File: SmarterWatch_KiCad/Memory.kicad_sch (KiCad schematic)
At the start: 7 parts, among them U12 M24C64-WMN6TP

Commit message: Clean Up
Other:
- moved on the sheet: J4, J5, R16, R17, R18

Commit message: order
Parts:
- removed J4, J5, J6: ~, Connector_Wire:SolderWirePad_1x01_SMD_2x4mm, symbol SmarterWatch_symbols_j:Solder_pad
- added U24, U25, U26: ~, symbol Custom:OpenJumper
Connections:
- net +3.3V: now also U24.1, U25.1, U26.1
- net at R17.2, U12.2 (A1): now also U25.2
- net at R16.2, U12.1 (A0): now also U26.2
- net at R18.2, U12.3 (A2): now also U24.2

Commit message: Minor Changes
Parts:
- renumbered R16 to R18, R17 to R19, R18 to R20, U26 to U12, U25 to U13, U24 to U14, U12 to U15
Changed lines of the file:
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@@
 		(dnp no)
 		(fields_autoplaced yes)
-		(property "Reference" "U26"
+		(property "Reference" "U12"
 			(at 120.65 73.66 0)
 			(effects
@@
 			(project "Smarter Watch Stuff"
 				(path "/52181fb0-1be8-41da-83b2-7d5a62778ff4/d294410d-228e-40f6-af22-786adbb6924d"
-					(reference "U26")
+					(reference "U12")
 					(unit 1)
 				)
@@
 		(dnp no)
 		(fields_autoplaced yes)
-		(property "Reference" "#PWR0101"
+		(property "Reference" "#PWR065"
 			(at 123.19 66.04 0)
 			(effects
@@
 			(project ""
 				(path "/52181fb0-1be8-41da-83b2-7d5a62778ff4/d294410d-228e-40f6-af22-786adbb6924d"
-					(reference "#PWR0101")
+					(reference "#PWR065")
 					(unit 1)
 				)
@@
 		(dnp no)
 		(fields_autoplaced yes)
-		(property "Reference" "#PWR061"
+		(property "Reference" "#PWR067"
 			(at 138.43 105.41 0)
 			(effects
@@
 			(project ""
 				(path "/52181fb0-1be8-41da-83b2-7d5a62778ff4/d294410d-228e-40f6-af22-786adbb6924d"
-					(reference "#PWR061")
+					(reference "#PWR067")
 					(unit 1)
 				)
@@
 		(dnp no)
 		(fields_autoplaced yes)
-		(property "Reference" "R17"
+		(property "Reference" "R19"
 			(at 114.3 85.09 90)
 			(effects
@@
 			(project "Smarter Watch Stuff"
 				(path "/52181fb0-1be8-41da-83b2-7d5a62778ff4/d294410d-228e-40f6-af22-786adbb6924d"
-					(reference "R17")
+					(reference "R19")
 					(unit 1)
 				)
@@
 		(dnp no)
 		(fields_autoplaced yes)
-		(property "Reference" "R16"
+		(property "Reference" "R18"
 			(at 114.3 82.55 90)
 			(effects
@@
 			(project ""
 				(path "/52181fb0-1be8-41da-83b2-7d5a62778ff4/d294410d-228e-40f6-af22-786adbb6924d"
-					(reference "R16")
+					(reference "R18")
 					(unit 1)
 				)
@@
 		(dnp no)
 		(fields_autoplaced yes)
-		(property "Reference" "#PWR060"
+		(property "Reference" "#PWR066"
 			(at 138.43 85.09 0)
 			(effects
@@
 			(project ""
 				(path "/52181fb0-1be8-41da-83b2-7d5a62778ff4/d294410d-228e-40f6-af22-786adbb6924d"
-					(reference "#PWR060")
+					(reference "#PWR066")
 					(unit 1)
 				)
@@
 		(dnp no)
 		(fields_autoplaced yes)
-		(property "Reference" "#PWR062"
+		(property "Reference" "#PWR068"
 			(at 154.94 93.98 0)
 			(effects
@@
 			(project "Smarter Watch Stuff"
 				(path "/52181fb0-1be8-41da-83b2-7d5a62778ff4/d294410d-228e-40f6-af22-786adbb6924d"
-					(reference "#PWR062")
+					(reference "#PWR068")
 					(unit 1)
 				)
@@
 		(dnp no)
 		(fields_autoplaced yes)
-		(property "Reference" "#PWR059"
+		(property "Reference" "#PWR064"
 			(at 102.87 91.44 0)
 			(effects
@@
 			(project "Smarter Watch Stuff"
 				(path "/52181fb0-1be8-41da-83b2-7d5a62778ff4/d294410d-228e-40f6-af22-786adbb6924d"
-					(reference "#PWR059")
+					(reference "#PWR064")
 					(unit 1)
 				)
@@
 		(dnp no)
 		(fields_autoplaced yes)
-		(property "Reference" "U24"
+		(property "Reference" "U14"
 			(at 135.89 73.66 0)
 			(effects
@@
 			(project "Smarter Watch Stuff"
 				(path "/52181fb0-1be8-41da-83b2-7d5a62778ff4/d294410d-228e-40f6-af22-786adbb6924d"
-					(reference "U24")
+					(reference "U14")
 					(unit 1)
 				)
@@
 		(dnp no)
 		(fields_autoplaced yes)
-		(property "Reference" "U12"
+		(property "Reference" "U15"
 			(at 140.5733 81.28 0)
 			(effects
@@
 			(project ""
 				(path "/52181fb0-1be8-41da-83b2-7d5a62778ff4/d294410d-228e-40f6-af22-786adbb6924d"
-					(reference "U12")
+					(reference "U15")
 					(unit 1)
 				)
@@
 		(on_board yes)
 		(dnp no)
-		(property "Reference" "R18"
+		(property "Reference" "R20"
 			(at 114.3 87.63 90)
 			(effects
@@
 			(project "Smarter Watch Stuff"
 				(path "/52181fb0-1be8-41da-83b2-7d5a62778ff4/d294410d-228e-40f6-af22-786adbb6924d"
-					(reference "R18")
+					(reference "R20")
 					(unit 1)
 				)
@@
 		(dnp no)
 		(fields_autoplaced yes)
-		(property "Reference" "U25"
+		(property "Reference" "U13"
 			(at 128.27 73.66 0)
 			(effects
@@
 			(project "Smarter Watch Stuff"
 				(path "/52181fb0-1be8-41da-83b2-7d5a62778ff4/d294410d-228e-40f6-af22-786adbb6924d"
-					(reference "U25")
-					(unit 1)
-				)
+					(reference "U13")
+					(unit 1)
+				)

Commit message: Footprint Stuff
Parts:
- U15: footprint Package_SO:SOIC-8_3.9x4.9mm_P1.27mm -> (none)
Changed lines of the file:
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@@
 			)
 		)
-		(property "Footprint" "Package_SO:SOIC-8_3.9x4.9mm_P1.27mm"
+		(property "Footprint" ""
 			(at 138.43 80.01 0)
 			(effects

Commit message: Foot
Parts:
- U15: footprint (none) -> Custom_Foot:SOIC127P600X175-8N
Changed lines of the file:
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@@
 			)
 		)
-		(property "Footprint" ""
+		(property "Footprint" "Custom_Foot:SOIC127P600X175-8N"
 			(at 138.43 80.01 0)
 			(effects

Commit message: Jumpers
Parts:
- U12, U13, U14: footprint (none) -> Custom_Foot:Jumper_NO
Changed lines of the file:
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@@
 			)
 		)
-		(property "Footprint" ""
+		(property "Footprint" "Custom_Foot:Jumper_NO"
 			(at 118.11 73.66 0)
 			(effects
@@
 			)
 		)
-		(property "Footprint" ""
+		(property "Footprint" "Custom_Foot:Jumper_NO"
 			(at 133.35 73.66 0)
 			(effects
@@
 			)
 		)
-		(property "Footprint" ""
+		(property "Footprint" "Custom_Foot:Jumper_NO"
 			(at 125.73 73.66 0)
 			(effects

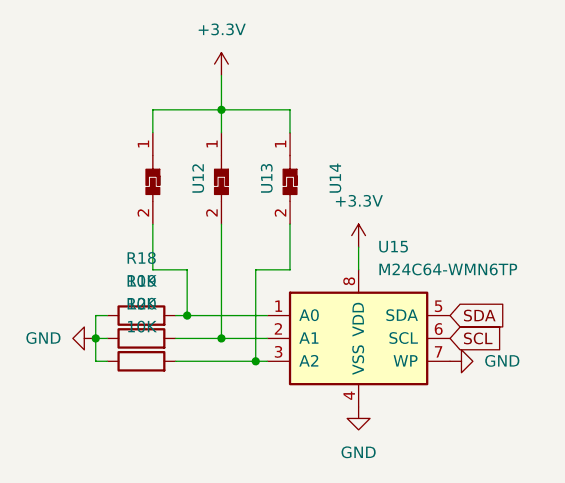
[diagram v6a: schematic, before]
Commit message: Label Jumpers
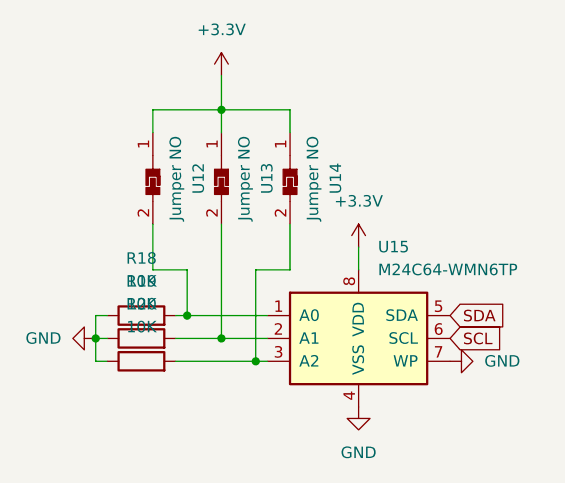
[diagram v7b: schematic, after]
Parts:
- U12, U13, U14: value ~ -> Jumper NO; footprint Custom_Foot:Jumper_NO -> (none)
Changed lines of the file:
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@@
 			)
 		)
-		(property "Value" "~"
+		(property "Value" "Jumper NO"
 			(at 118.11 73.66 0)
 			(effects
@@
 			)
 		)
-		(property "Footprint" "Custom_Foot:Jumper_NO"
+		(property "Footprint" ""
 			(at 118.11 73.66 0)
 			(effects
@@
 			)
 		)
-		(property "Value" "~"
+		(property "Value" "Jumper NO"
 			(at 133.35 73.66 0)
 			(effects
@@
 			)
 		)
-		(property "Footprint" "Custom_Foot:Jumper_NO"
+		(property "Footprint" ""
 			(at 133.35 73.66 0)
 			(effects
@@
 			)
 		)
-		(property "Value" "~"
+		(property "Value" "Jumper NO"
 			(at 125.73 73.66 0)
 			(effects
@@
 			)
 		)
-		(property "Footprint" "Custom_Foot:Jumper_NO"
+		(property "Footprint" ""
 			(at 125.73 73.66 0)
 			(effects

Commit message: added pad to symbol
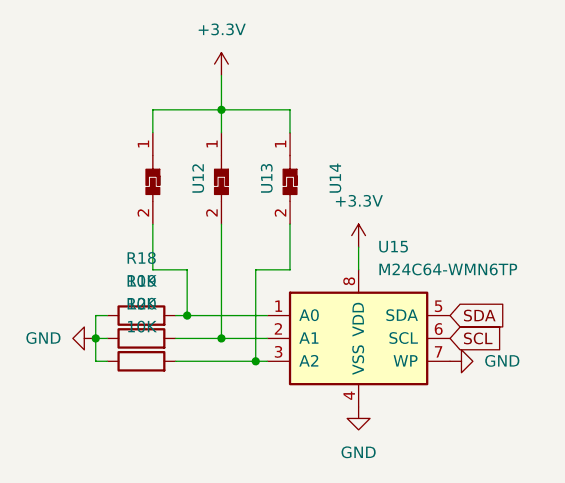
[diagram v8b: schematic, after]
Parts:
- U12, U13, U14: value Jumper NO -> ~; footprint (none) -> Custom_Foot:Jumper_NO
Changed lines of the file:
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@@
 			)
 		)
-		(property "Value" "Jumper NO"
+		(property "Value" "~"
 			(at 118.11 73.66 0)
 			(effects
@@
 			)
 		)
-		(property "Footprint" ""
+		(property "Footprint" "Custom_Foot:Jumper_NO"
 			(at 118.11 73.66 0)
 			(effects
@@
 			)
 		)
-		(property "Value" "Jumper NO"
+		(property "Value" "~"
 			(at 133.35 73.66 0)
 			(effects
@@
 			)
 		)
-		(property "Footprint" ""
+		(property "Footprint" "Custom_Foot:Jumper_NO"
 			(at 133.35 73.66 0)
 			(effects
@@
 			)
 		)
-		(property "Value" "Jumper NO"
+		(property "Value" "~"
 			(at 125.73 73.66 0)
 			(effects
@@
 			)
 		)
-		(property "Footprint" ""
+		(property "Footprint" "Custom_Foot:Jumper_NO"
 			(at 125.73 73.66 0)
 			(effects
